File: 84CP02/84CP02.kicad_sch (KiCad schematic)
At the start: 7 parts, among them J1 Conn_01x30, J2 Conn_01x30, J3 Conn_02x05_Odd_Even, J4 Conn_02x03_Odd_Even, U1 XC9572XL-VQ64

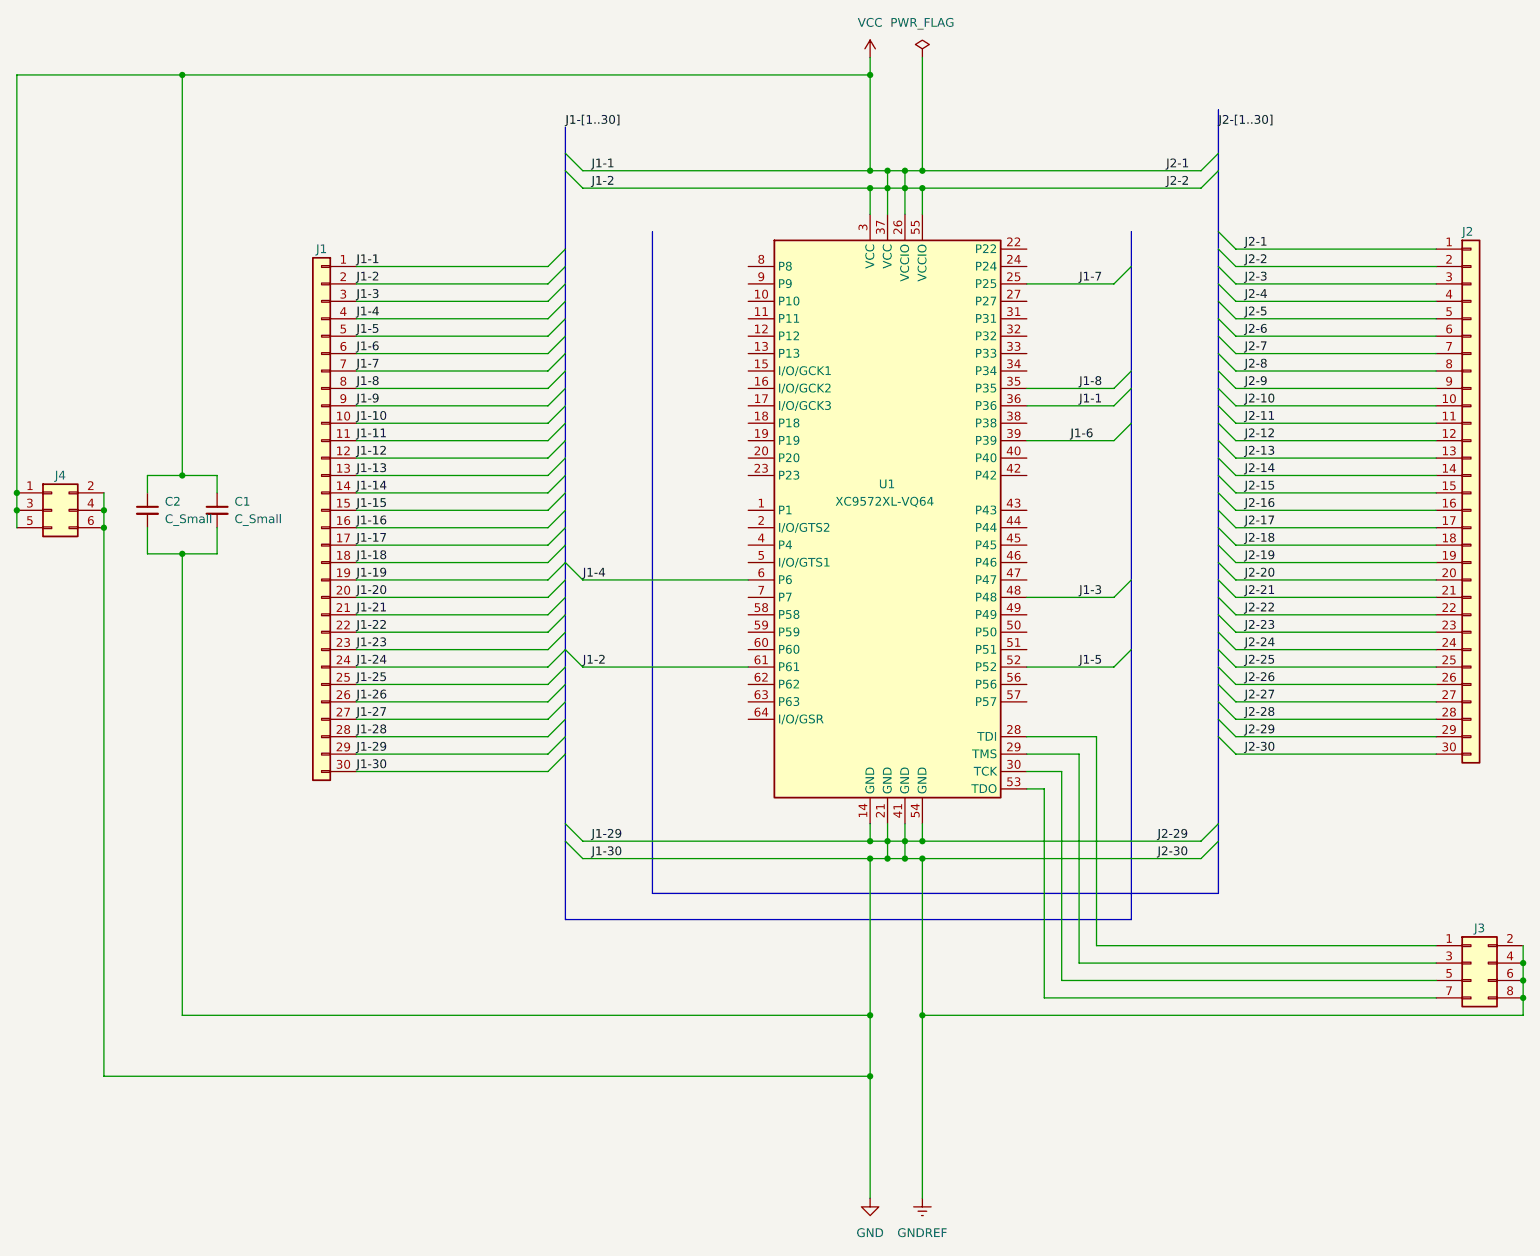
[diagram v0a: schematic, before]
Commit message: Again revise pin mapping table
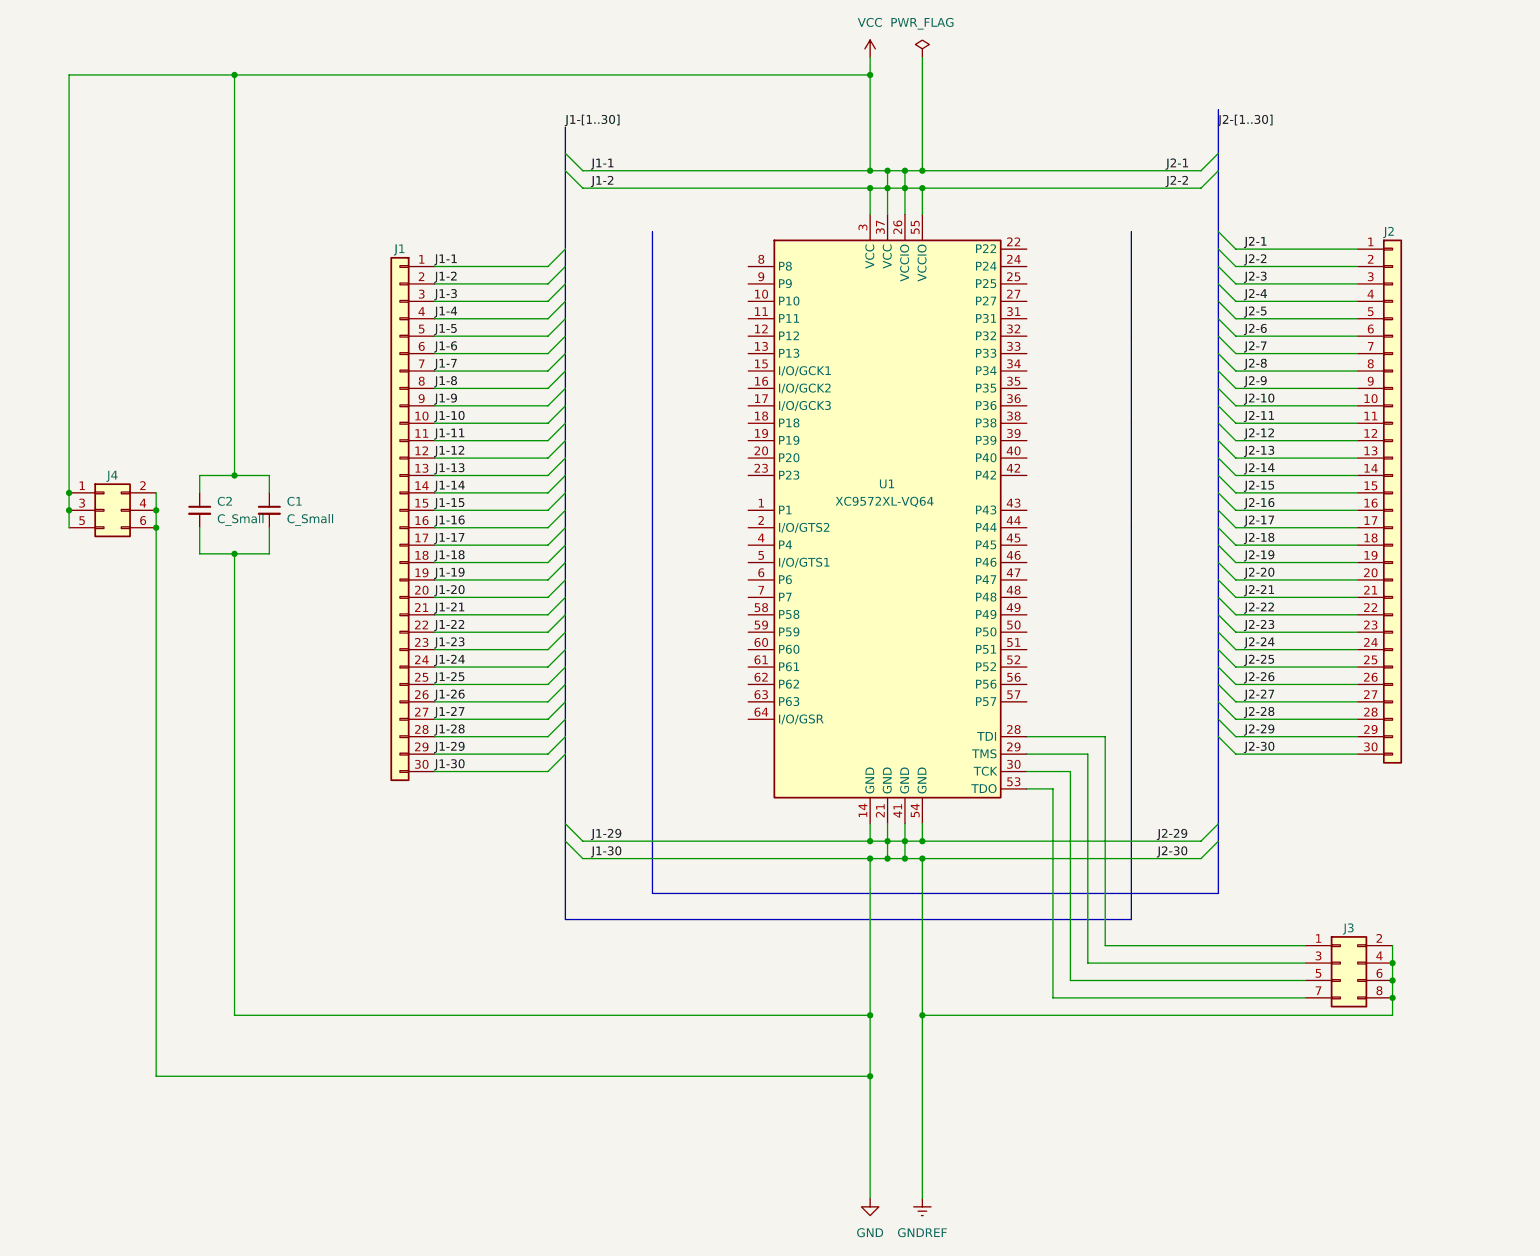
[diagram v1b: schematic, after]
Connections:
- net J1-3: no longer U1.48 (P48)
- net J1-4: no longer U1.6 (P6)
- net J1-5: no longer U1.52 (P52)
- net J1-6: no longer U1.39 (P39)
- net J1-7: no longer U1.25 (P25)
- net J1-8: no longer U1.35 (P35)
- net VCC: no longer U1.36 (P36), U1.61 (P61)
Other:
- title: 84CP01 Scrambled Breakout Board -> 84CP02 Descrambled 2x16 Input / 16 Output / 4 Control
- moved on the sheet: C1, C2, J1, J2, J3, J4

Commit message: Continuing development
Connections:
- net J1-10: now also U1.35 (P35)
- net J1-11: now also U1.8 (P8)
- net J1-12: now also U1.45 (P45)
- net J1-13: now also U1.2 (I/O/GTS2)
- net J1-14: now also U1.5 (I/O/GTS1)
- net J1-15: now also U1.31 (P31)
- net J1-16: now also U1.56 (P56)
- net J1-17: now also U1.34 (P34)
- net J1-18: now also U1.58 (P58)
- net J1-19: now also U1.64 (I/O/GSR)
- net J1-20: now also U1.59 (P59)
- net J1-21: now also U1.46 (P46)
- net J1-22: now also U1.33 (P33)
- net J1-23: now also U1.16 (I/O/GCK2)
- net J1-24: now also U1.47 (P47)
- net J1-25: now also U1.32 (P32)
- net J1-26: now also U1.44 (P44)
- net J1-27: now also U1.9 (P9)
- net J1-28: now also U1.57 (P57)
- net J1-3: now also U1.36 (P36)
- net J1-4: now also U1.61 (P61)
- net J1-5: now also U1.48 (P48)
- net J1-6: now also U1.6 (P6)
- net J1-7: now also U1.52 (P52)
- net J1-8: now also U1.39 (P39)
- net J1-9: now also U1.25 (P25)
- net J2-27: now also U1.19 (P19)
- net J2-28: now also U1.12 (P12)

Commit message: First attempts at routing the CP02 baseboard
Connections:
- net J2-10: now also U1.50 (P50)
- net J2-11: now also U1.42 (P42)
- net J2-12: now also U1.27 (P27)
- net J2-13: now also U1.13 (P13)
- net J2-14: now also U1.23 (P23)
- net J2-15: now also U1.40 (P40)
- net J2-16: now also U1.10 (P10)
- net J2-17: now also U1.1 (P1)
- net J2-18: now also U1.7 (P7)
- net J2-19: now also U1.17 (I/O/GCK3)
- net J2-20: now also U1.38 (P38)
- net J2-21: now also U1.63 (P63)
- net J2-22: now also U1.15 (I/O/GCK1)
- net J2-23: now also U1.11 (P11)
- net J2-24: now also U1.60 (P60)
- net J2-25: now also U1.18 (P18)
- net J2-26: now also U1.20 (P20)
- net J2-3: now also U1.62 (P62)
- net J2-4: now also U1.43 (P43)
- net J2-5: now also U1.22 (P22)
- net J2-6: now also U1.24 (P24)
- net J2-7: now also U1.49 (P49)
- net J2-8: now also U1.4 (P4)
- net J2-9: now also U1.51 (P51)
